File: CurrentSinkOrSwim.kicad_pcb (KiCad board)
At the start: 2 copper layers, 41.7 x 47.8 mm, 23 parts, among them P1 CONN_01X01, P101 CONN_01X02, P102 CONN_01X03, P103 CONN_01X02, Q401 BUK9575, U201 LMV358, U301 LM2931D-R

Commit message: deleted orphaned libraries in EEschema, imported updated netlist into PCBNew and checked for errors
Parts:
- C201, C301, C302: value C -> .1
- D201: value DIODE -> 1N4148
- P1: value CONN_01X01 -> HEATSINK
- U301: value LM2931D-R -> LM2931
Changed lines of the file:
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@@
-(kicad_pcb (version 4) (host pcbnew 0.201502010101+5397~21~ubuntu14.04.1-product)
+(kicad_pcb (version 4) (host pcbnew 4.0.2-stable)
   (general
     (links 42)
@@
       (effects (font (size 1 1) (thickness 0.15)) (justify mirror))
     )
-    (fp_text value C (at 0 -0.381 270) (layer B.SilkS) hide
+    (fp_text value .1 (at 0 -0.381 270) (layer B.SilkS) hide
       (effects (font (size 1 1) (thickness 0.15)) (justify mirror))
     )
@@
       (effects (font (size 1 1) (thickness 0.15)) (justify mirror))
     )
-    (fp_text value C (at 0 -0.381 90) (layer B.SilkS) hide
+    (fp_text value .1 (at 0 -0.381 90) (layer B.SilkS) hide
       (effects (font (size 1 1) (thickness 0.15)) (justify mirror))
     )
@@
       (effects (font (size 1 1) (thickness 0.15)) (justify mirror))
     )
-    (fp_text value C (at 0 -0.381) (layer B.SilkS) hide
+    (fp_text value .1 (at 0 -0.381) (layer B.SilkS) hide
       (effects (font (size 1 1) (thickness 0.15)) (justify mirror))
     )
@@
       (effects (font (size 1 1) (thickness 0.15)))
     )
-    (fp_text value DIODE (at 0 1.7 270) (layer F.SilkS) hide
+    (fp_text value 1N4148 (at 0 1.7 270) (layer F.SilkS) hide
       (effects (font (size 1 1) (thickness 0.15)))
     )
@@
       (effects (font (size 1 1) (thickness 0.15)))
     )
-    (fp_text value LM2931D-R (at 0 1.27 270) (layer F.SilkS) hide
+    (fp_text value LM2931 (at 0 1.27 270) (layer F.SilkS) hide
       (effects (font (size 1 1) (thickness 0.15)))
     )
@@
       (effects (font (size 1.5 1.5) (thickness 0.15)))
     )
-    (fp_text value CONN_01X01 (at 0 -6.35) (layer F.Fab) hide
+    (fp_text value HEATSINK (at 0 -6.35) (layer F.Fab) hide
       (effects (font (size 1.5 1.5) (thickness 0.15)))
     )

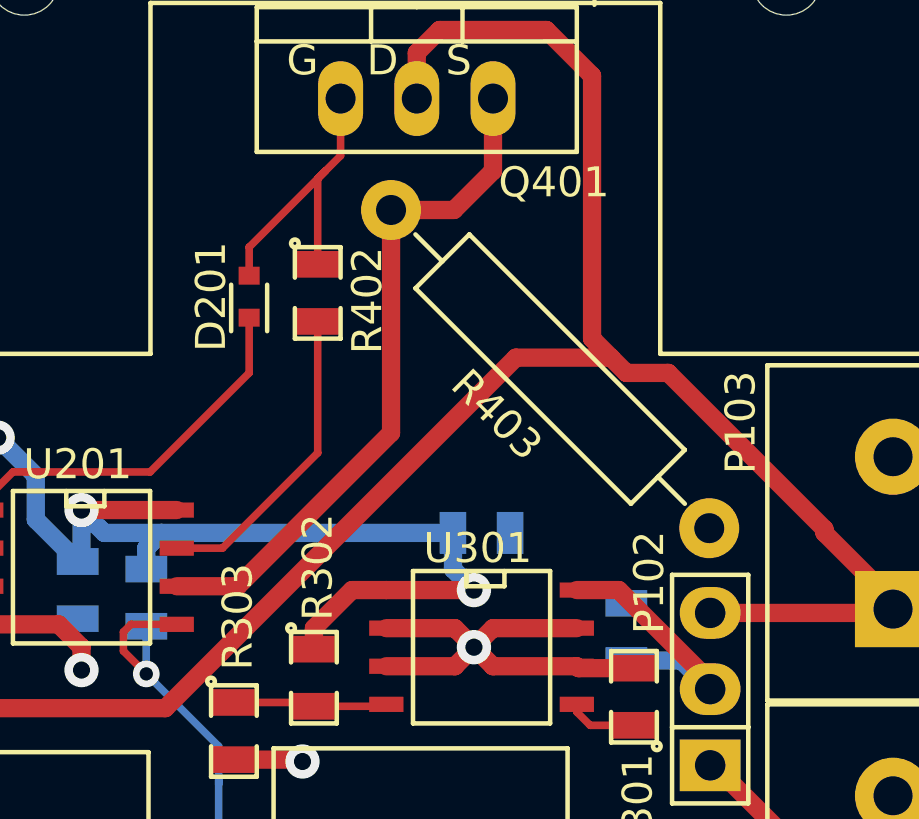
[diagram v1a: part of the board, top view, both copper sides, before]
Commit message: added 100uF pcb footprint and misc comments
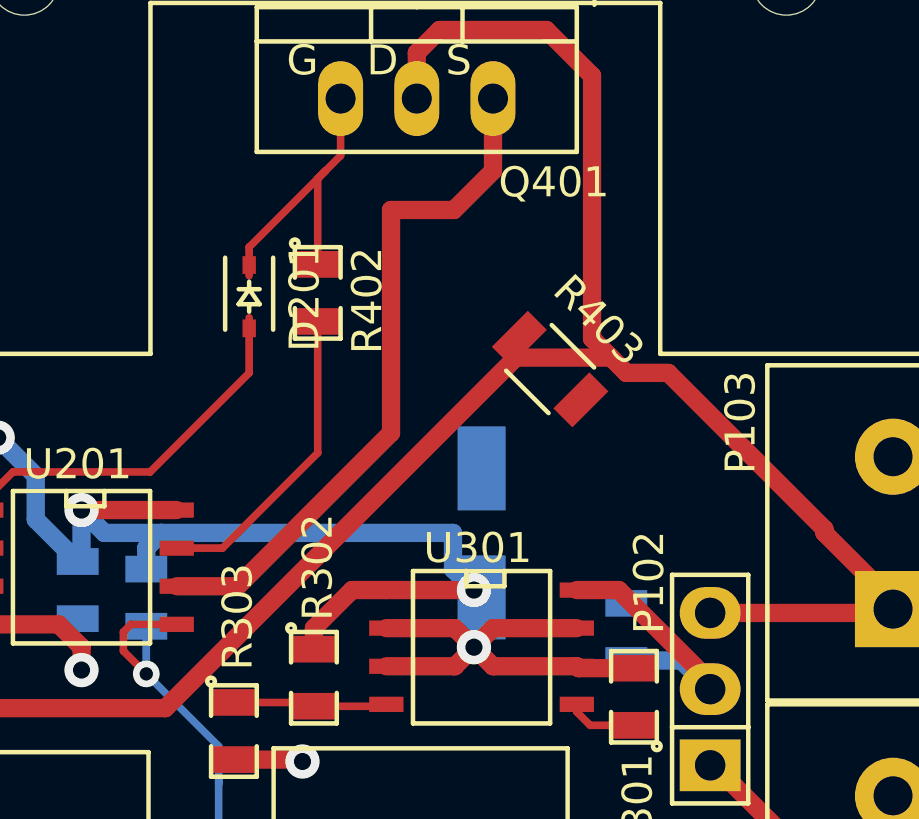
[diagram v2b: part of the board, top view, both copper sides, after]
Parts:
- C302: value .1 -> 100; footprint SMD_Packages:SMD-0805 -> Current:PCE3867CT-ND
- D201: footprint SMD_Packages:SOD-523 -> Diodes_SMD:SOD-323
- R201: value 28.7K -> 3.3K
- R403: footprint Resistors_ThroughHole:Resistor_Horizontal_RM15mm -> Resistors_SMD:R_1206
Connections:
- D201 pad 1: /Current Control/FET_Gate -> Net-(D201-Pad1)
- D201 pad 2: Net-(D201-Pad2) -> /Current Control/FET_Gate
- U201 pad 1: Net-(D201-Pad2) -> Net-(D201-Pad1)
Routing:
- net Net-(Q401-PadS): track 23.0 -> 55.3 mm
- net /Current Control/Current_Sink+: track 63.5 -> 31.3 mm
- net Net-(D201-Pad2): track 12.7 -> 0.00 mm
- net Net-(D201-Pad1): track 0.00 -> 12.7 mm
- net 2.7V: track 35.3 -> 34.3 mm, vias 3 -> 2
- net GND: track 24.5 -> 25.4 mm, vias 4 -> 5

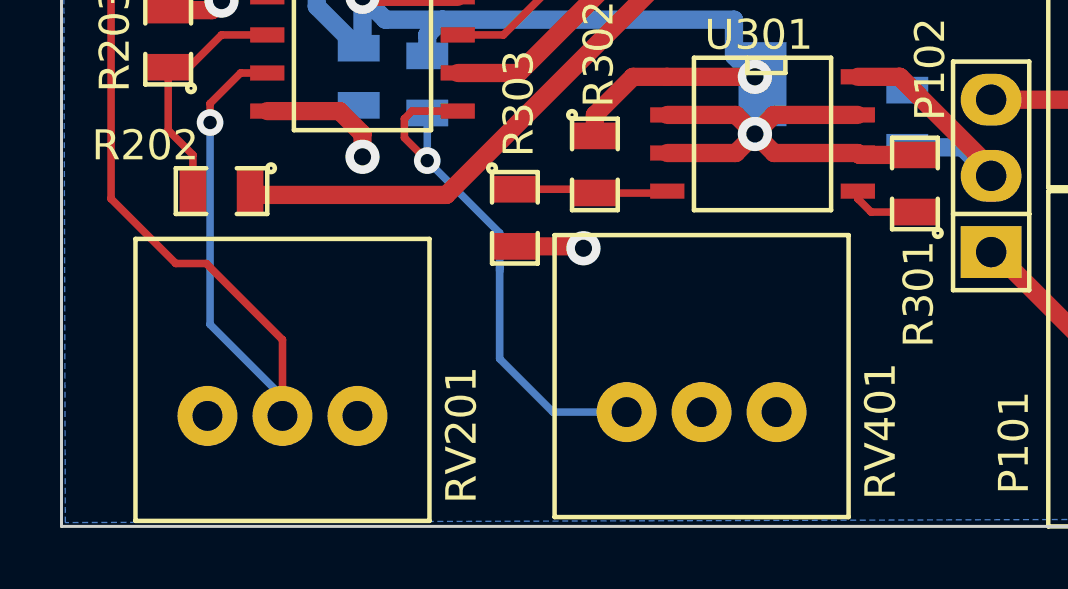
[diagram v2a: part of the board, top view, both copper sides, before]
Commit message: update pot footprints to have circular mounting holes
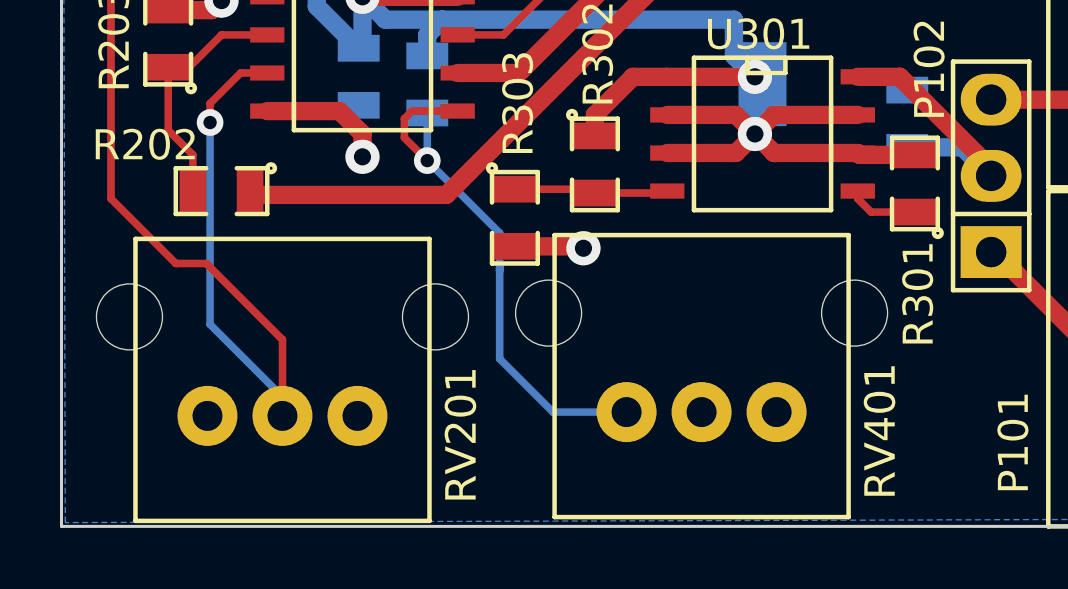
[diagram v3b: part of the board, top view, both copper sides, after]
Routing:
- net Net-(Q401-PadS): track 55.3 -> 52.4 mm
- net /Current Control/Current_Sink+: track 31.3 -> 34.1 mm
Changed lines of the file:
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@@
     (links 42)
     (no_connects 9)
-    (area 106.121999 35.763999 147.878001 83.616001)
+    (area 105.817599 35.434199 148.182401 89.152801)
     (thickness 1.6)
     (drawings 5)
@@
       (xy 2.522392 -2.829784) (xy 2.75031 -2.286) (xy 2.775091 -2.176038) (xy 2.775091 -2.176038)) (layer F.SilkS) (width 0.1))
   )
-  (module Current:P090L-02F25BR10K (layer F.Cu)
-    (at 127.508 79.756)
-    (fp_text reference RV401 (at 5.969 0.635 90) (layer F.SilkS)
-      (effects (font (size 1.016 1.016) (thickness 0.15)))
-    )
-    (fp_text value 10K (at 0 -9.906) (layer F.Fab) hide
-      (effects (font (size 1.5 1.5) (thickness 0.15)))
-    )
-    (fp_line (start -1.778 3.556) (end -1.778 8.89) (layer Eco1.User) (width 0.15))
-    (fp_line (start -1.778 8.89) (end 2.54 8.89) (layer Eco1.User) (width 0.15))
-    (fp_line (start 2.54 8.89) (end 2.54 3.556) (layer Eco1.User) (width 0.15))
-    (fp_line (start -4.9 -5.9) (end 4.9 -5.9) (layer F.SilkS) (width 0.15))
-    (fp_line (start -4.9 3.5) (end 4.9 3.5) (layer F.SilkS) (width 0.15))
-    (fp_line (start 4.9 -5.9) (end 4.9 3.5) (layer F.SilkS) (width 0.15))
-    (fp_line (start -4.9 -5.9) (end -4.9 3.5) (layer F.SilkS) (width 0.15))
-    (pad 3 thru_hole circle (at 2.5 0) (size 2 2) (drill 1) (layers *.Cu *.Mask F.SilkS)
-      (net 15 "Net-(RV401-Pad3)"))
-    (pad 2 thru_hole circle (at 0 0) (size 2 2) (drill 1) (layers *.Cu *.Mask F.SilkS)
-      (net 2 GND))
-    (pad 1 thru_hole circle (at -2.5 0) (size 2 2) (drill 1) (layers *.Cu *.Mask F.SilkS)
-      (net 13 "Net-(R401-Pad2)"))
-    (pad "" np_thru_hole oval (at 5.1 -3.3) (size 2 2.2) (drill oval 2 2.2) (layers *.Cu *.Mask F.SilkS))
-    (pad "" np_thru_hole oval (at -5.1 -3.3) (size 2 2.2) (drill oval 2 2.2) (layers *.Cu *.Mask F.SilkS))
-  )
-  (module Current:P090L-02F25BR10K (layer F.Cu)
-    (at 113.538 79.883)
-    (fp_text reference RV201 (at 5.969 0.635 90) (layer F.SilkS)
-      (effects (font (size 1.016 1.016) (thickness 0.15)))
-    )
-    (fp_text value 10K (at 0 -9.906) (layer F.Fab) hide
-      (effects (font (size 1.5 1.5) (thickness 0.15)))
-    )
-    (fp_line (start -1.778 3.556) (end -1.778 8.89) (layer Eco1.User) (width 0.15))
-    (fp_line (start -1.778 8.89) (end 2.54 8.89) (layer Eco1.User) (width 0.15))
-    (fp_line (start 2.54 8.89) (end 2.54 3.556) (layer Eco1.User) (width 0.15))
-    (fp_line (start -4.9 -5.9) (end 4.9 -5.9) (layer F.SilkS) (width 0.15))
-    (fp_line (start -4.9 3.5) (end 4.9 3.5) (layer F.SilkS) (width 0.15))
-    (fp_line (start 4.9 -5.9) (end 4.9 3.5) (layer F.SilkS) (width 0.15))
-    (fp_line (start -4.9 -5.9) (end -4.9 3.5) (layer F.SilkS) (width 0.15))
-    (pad 3 thru_hole circle (at 2.5 0) (size 2 2) (drill 1) (layers *.Cu *.Mask F.SilkS)
-      (net 2 GND))
-    (pad 2 thru_hole circle (at 0 0) (size 2 2) (drill 1) (layers *.Cu *.Mask F.SilkS)
-      (net 12 "Net-(R201-Pad2)"))
-    (pad 1 thru_hole circle (at -2.5 0) (size 2 2) (drill 1) (layers *.Cu *.Mask F.SilkS)
-      (net 14 "Net-(RV201-Pad1)"))
-    (pad "" np_thru_hole oval (at 5.1 -3.3) (size 2 2.2) (drill oval 2 2.2) (layers *.Cu *.Mask F.SilkS))
-    (pad "" np_thru_hole oval (at -5.1 -3.3) (size 2 2.2) (drill oval 2 2.2) (layers *.Cu *.Mask F.SilkS))
-  )
   (module Current:PCE3867CT-ND (layer B.Cu)
     (at 129.54 66.675)
@@
       (rotate (xyz 0 0 0))
     )
+  )
+  (module Current:P090L-02F25BR10K (layer F.Cu)
+    (at 113.538 79.883)
+    (fp_text reference RV201 (at 5.969 0.635 90) (layer F.SilkS)
+      (effects (font (size 1.016 1.016) (thickness 0.15)))
+    )
+    (fp_text value 10K (at 0 -9.906) (layer F.Fab) hide
+      (effects (font (size 1.5 1.5) (thickness 0.15)))
+    )
+    (fp_line (start -1.778 3.556) (end -1.778 8.89) (layer Eco1.User) (width 0.15))
+    (fp_line (start -1.778 8.89) (end 2.54 8.89) (layer Eco1.User) (width 0.15))
+    (fp_line (start 2.54 8.89) (end 2.54 3.556) (layer Eco1.User) (width 0.15))
+    (fp_line (start -4.9 -5.9) (end 4.9 -5.9) (layer F.SilkS) (width 0.15))
+    (fp_line (start -4.9 3.5) (end 4.9 3.5) (layer F.SilkS) (width 0.15))
+    (fp_line (start 4.9 -5.9) (end 4.9 3.5) (layer F.SilkS) (width 0.15))
+    (fp_line (start -4.9 -5.9) (end -4.9 3.5) (layer F.SilkS) (width 0.15))
+    (pad 3 thru_hole circle (at 2.5 0) (size 2 2) (drill 1) (layers *.Cu *.Mask F.SilkS)
+      (net 2 GND))
+    (pad 2 thru_hole circle (at 0 0) (size 2 2) (drill 1) (layers *.Cu *.Mask F.SilkS)
+      (net 12 "Net-(R201-Pad2)"))
+    (pad 1 thru_hole circle (at -2.5 0) (size 2 2) (drill 1) (layers *.Cu *.Mask F.SilkS)
+      (net 14 "Net-(RV201-Pad1)"))
+    (pad "" np_thru_hole circle (at 5.1 -3.3) (size 2.2 2.2) (drill 2.2) (layers *.Cu *.Mask F.SilkS))
+    (pad "" np_thru_hole circle (at -5.1 -3.3) (size 2.2 2.2) (drill 2.2) (layers *.Cu *.Mask F.SilkS))
+  )
+  (module Current:P090L-02F25BR10K (layer F.Cu)
+    (at 127.508 79.756)
+    (fp_text reference RV401 (at 5.969 0.635 90) (layer F.SilkS)
+      (effects (font (size 1.016 1.016) (thickness 0.15)))
+    )
+    (fp_text value 10K (at 0 -9.906) (layer F.Fab) hide
+      (effects (font (size 1.5 1.5) (thickness 0.15)))
+    )
+    (fp_line (start -1.778 3.556) (end -1.778 8.89) (layer Eco1.User) (width 0.15))
+    (fp_line (start -1.778 8.89) (end 2.54 8.89) (layer Eco1.User) (width 0.15))
+    (fp_line (start 2.54 8.89) (end 2.54 3.556) (layer Eco1.User) (width 0.15))
+    (fp_line (start -4.9 -5.9) (end 4.9 -5.9) (layer F.SilkS) (width 0.15))
+    (fp_line (start -4.9 3.5) (end 4.9 3.5) (layer F.SilkS) (width 0.15))
+    (fp_line (start 4.9 -5.9) (end 4.9 3.5) (layer F.SilkS) (width 0.15))
+    (fp_line (start -4.9 -5.9) (end -4.9 3.5) (layer F.SilkS) (width 0.15))
+    (pad 3 thru_hole circle (at 2.5 0) (size 2 2) (drill 1) (layers *.Cu *.Mask F.SilkS)
+      (net 15 "Net-(RV401-Pad3)"))
+    (pad 2 thru_hole circle (at 0 0) (size 2 2) (drill 1) (layers *.Cu *.Mask F.SilkS)
+      (net 2 GND))
+    (pad 1 thru_hole circle (at -2.5 0) (size 2 2) (drill 1) (layers *.Cu *.Mask F.SilkS)
+      (net 13 "Net-(R401-Pad2)"))
+    (pad "" np_thru_hole circle (at 5.1 -3.3) (size 2.2 2.2) (drill 2.2) (layers *.Cu *.Mask F.SilkS))
+    (pad "" np_thru_hole circle (at -5.1 -3.3) (size 2.2 2.2) (drill 2.2) (layers *.Cu *.Mask F.SilkS))
   )
   (gr_text "Current Sink\nOr Swim" (at 126.746 44.577) (layer F.SilkS)
@@
   (segment (start 143.129 69.342) (end 143.256 69.215) (width 0.6096) (layer F.Cu) (net 6))
   (segment (start 137.16 69.342) (end 143.129 69.342) (width 0.6096) (layer F.Cu) (net 6))
+  (segment (start 134.366 61.341) (end 133.858 60.833) (width 0.6096) (layer F.Cu) (net 6))
+  (segment (start 133.223 51.435) (end 131.699 49.911) (width 0.6096) (layer F.Cu) (net 6))
   (segment (start 130.683 60.833) (end 133.858 60.833) (width 0.6096) (layer F.Cu) (net 7))
   (segment (start 130.683 60.833) (end 118.999 72.517) (width 0.6096) (layer F.Cu) (net 7))
-  (segment (start 134.366 61.341) (end 133.858 60.833) (width 0.6096) (layer F.Cu) (net 7))
   (segment (start 133.858 60.833) (end 133.223 60.198) (width 0.6096) (layer F.Cu) (net 7))
   (segment (start 133.223 60.198) (end 133.223 51.435) (width 0.6096) (layer F.Cu) (net 7))
-  (segment (start 133.223 51.435) (end 131.699 49.911) (width 0.6096) (layer F.Cu) (net 7))
   (segment (start 119.38 68.453) (end 121.412 68.453) (width 0.6096) (layer F.Cu) (net 7))
   (segment (start 126.522699 63.342301) (end 126.522699 55.910699) (width 0.6096) (layer F.Cu) (net 7))

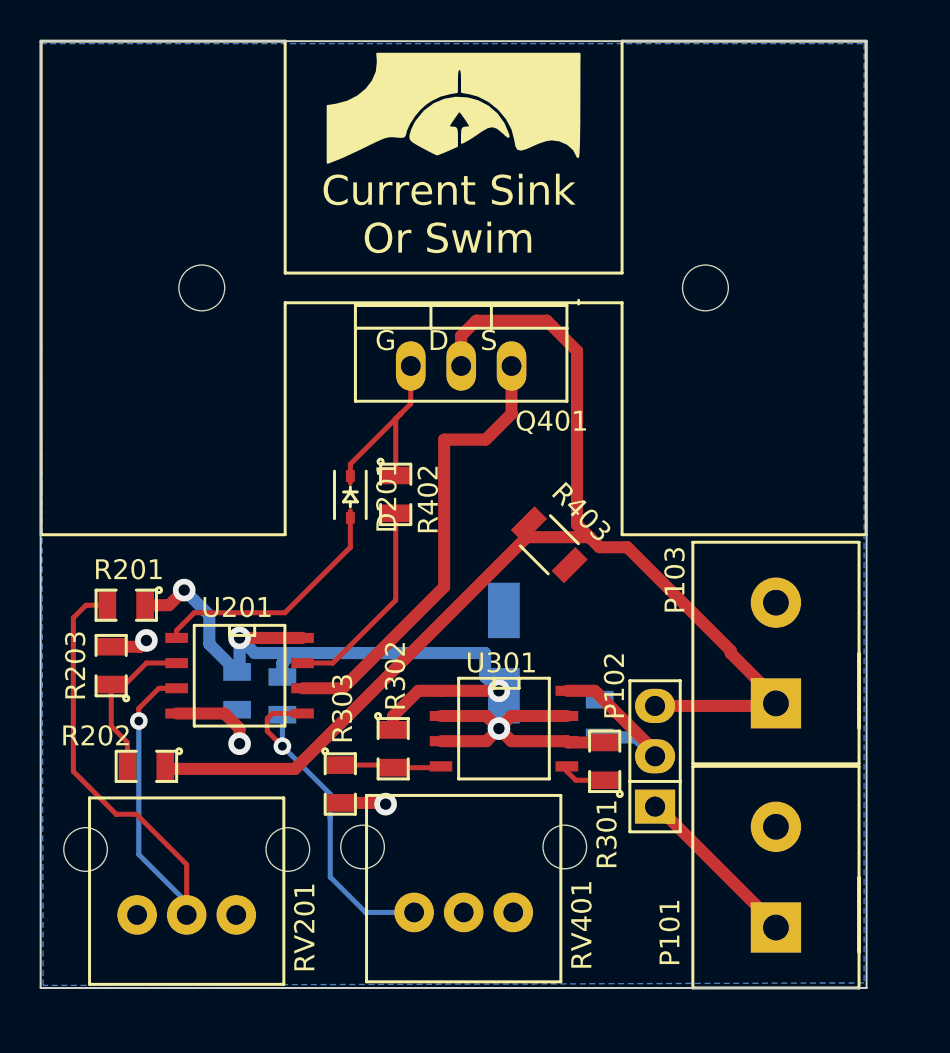
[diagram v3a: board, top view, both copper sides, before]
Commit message: initial component placement on the pcb
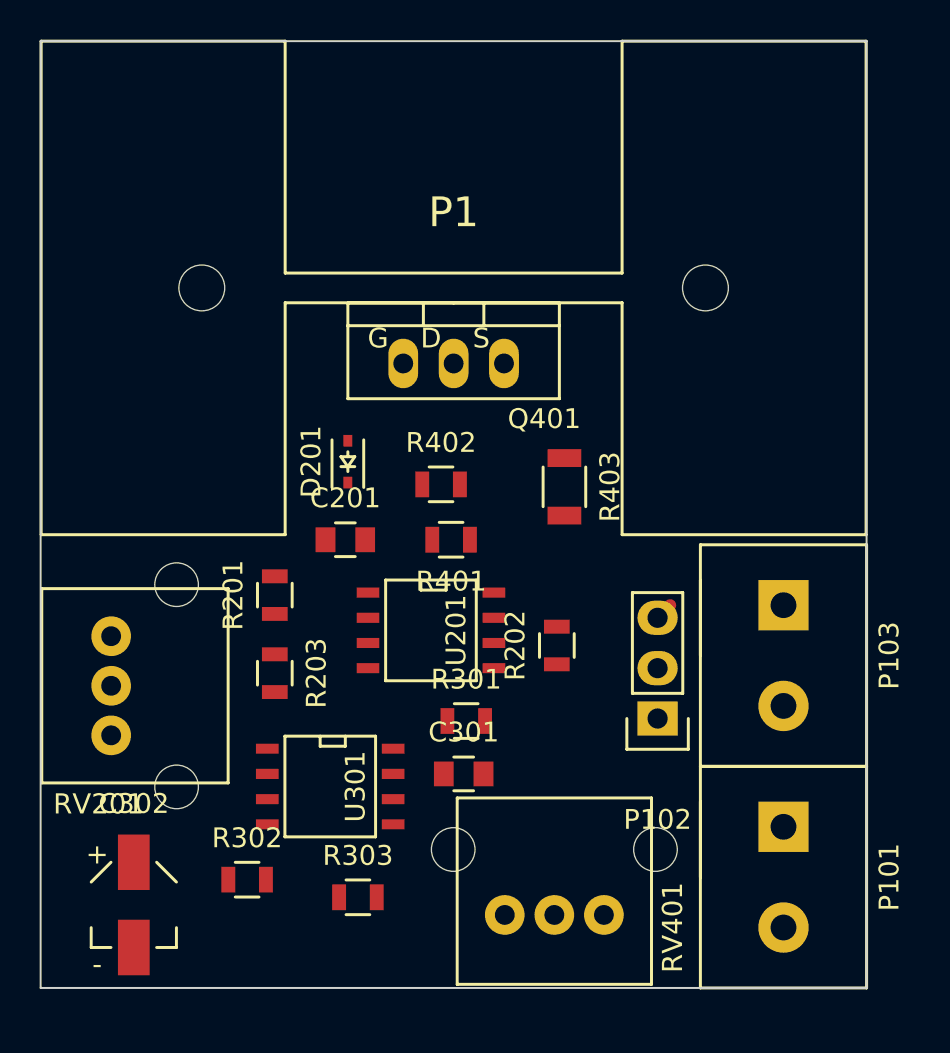
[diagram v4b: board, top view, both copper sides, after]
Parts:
- removed G***: LOGO, Current:CSOS
- C201, C301: footprint SMD_Packages:SMD-0805 -> Capacitors_SMD:C_0805; moved to F.Cu
- C302: moved to F.Cu
- Q401: footprint Transistors_TO-220:TO-220_FET-GDS_Vertical -> Current:TO-220_FET-GDS_Vertical
- R201, R202, R203, R301, R302, R303, R402: footprint SMD_Packages:SMD-0805 -> Resistors_SMD:R_0805
- R401: footprint SMD_Packages:SMD-0805 -> Resistors_SMD:R_0805; moved to F.Cu
- moved C302 22.6 mm to (110.9, 79.4), turned to 180 degrees
- moved R202 21.6 mm to (132.2, 66.3), turned to 90 degrees
- moved RV201 12.2 mm to (109.7, 68.3), turned to 270 degrees
- moved R401 11.6 mm to (126.9, 61.0), turned to 180 degrees
- moved U201 9.92 mm to (125.9, 65.5)
- moved R302 9.89 mm to (116.6, 78.1), turned to 0 degrees
- moved C201 9.37 mm to (121.5, 61.0), turned to 0 degrees
- moved U301 9.24 mm to (120.8, 73.4)
- moved R203 8.26 mm to (118.0, 67.7), turned to 270 degrees
- moved R201 7.51 mm to (118.0, 63.8), turned to 90 degrees
- moved C301 7.41 mm to (127.5, 72.8), turned to 0 degrees
- moved R301 7.27 mm to (127.6, 70.1), turned to 0 degrees
- moved R303 5.78 mm to (122.2, 79.0), turned to 0 degrees
- moved RV401 4.57 mm to (132.1, 79.9)
- moved R403 3.02 mm to (132.6, 58.3), turned to 270 degrees
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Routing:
- net Net-(Q401-PadS): track 52.4 -> 0.00 mm
- net 2.7V: track 34.3 -> 0.00 mm, vias 2 -> 0
- net Net-(R201-Pad2): track 33.7 -> 0.00 mm, vias 1 -> 0
- net /Current Control/Current_Sink+: track 34.1 -> 1.66 mm
- net GND: track 25.4 -> 0.00 mm, vias 5 -> 0
- net Net-(R401-Pad2): track 17.9 -> 0.00 mm, vias 1 -> 0
- net Net-(D201-Pad1): track 12.7 -> 0.00 mm
- net Net-(R402-Pad2): track 10.4 -> 0.00 mm
- net /Current Control/FET_Gate: track 10.4 -> 0.00 mm
- net /Power Regulation/Vin: track 10.0 -> 0.00 mm
- net Net-(P101-Pad1): track 8.70 -> 0.00 mm
- net Net-(R202-Pad2): track 8.31 -> 0.00 mm
- net Net-(R302-Pad2): track 5.16 -> 0.00 mm
- net Net-(R301-Pad1): track 2.34 -> 0.00 mm
- removed copper zone on B.Cu, net GND
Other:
- board text removed: "Current Sink Or Swim"
